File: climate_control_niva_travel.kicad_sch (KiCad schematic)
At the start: 12 parts, among them J2 SWD-отладка 1x04, U1 STM32F103RCT6

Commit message: реализована 2я занятость клетки
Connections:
- net LED_RECIRC_DRV is gone; now on net X_PWR/VCC_3V3: U1.10 (PC2)
- net X_SEN_CABIN/NTC_CABIN is gone; now on net X_PWR/VCC_3V3: U1.16 (PA2)
- net X_SEN_HEAT/NTC_HEAT is gone; now on net HEAT_FAN_PWM_CTL: U1.17 (PA3)
- net X_UI/LED_DRY_GLASS_DRV is gone; now on net HEAT_FAN_PWM_CTL: U1.3 (PC14)
- net HEAT_FAN_PWM_CTL: now also U1.2 (PC13)
- net X_M1/IN1: no longer U1.43 (PA10)
- net X_M2/IN1: no longer U1.45 (PA12)
- net X_M3/FB: no longer U1.27 (PB1)
- net X_M3/IN1: no longer U1.58 (PB6)
- net X_M4/IN1: no longer U1.2 (PC13)
- net X_UI/LED_DEFROST_GLASS_DRV: no longer C10.1, FB1.2, J2.2 (Pin_2), U1.13 (VDDA), U1.46 (PA13)
- net M_FAN_CTL renamed X_SEN_CABIN/M_FAN_CTL
- new net: C10.1, FB1.2, U1.13 (VDDA)
- new net: J2.2 (Pin_2), U1.46 (PA13)
- new net X_M1/IN2: U1.43 (PA10)
- new net X_M2/IN2: U1.45 (PA12)
- new net X_M3/IN2: U1.58 (PB6)
- new net X_M4/FB: U1.27 (PB1)

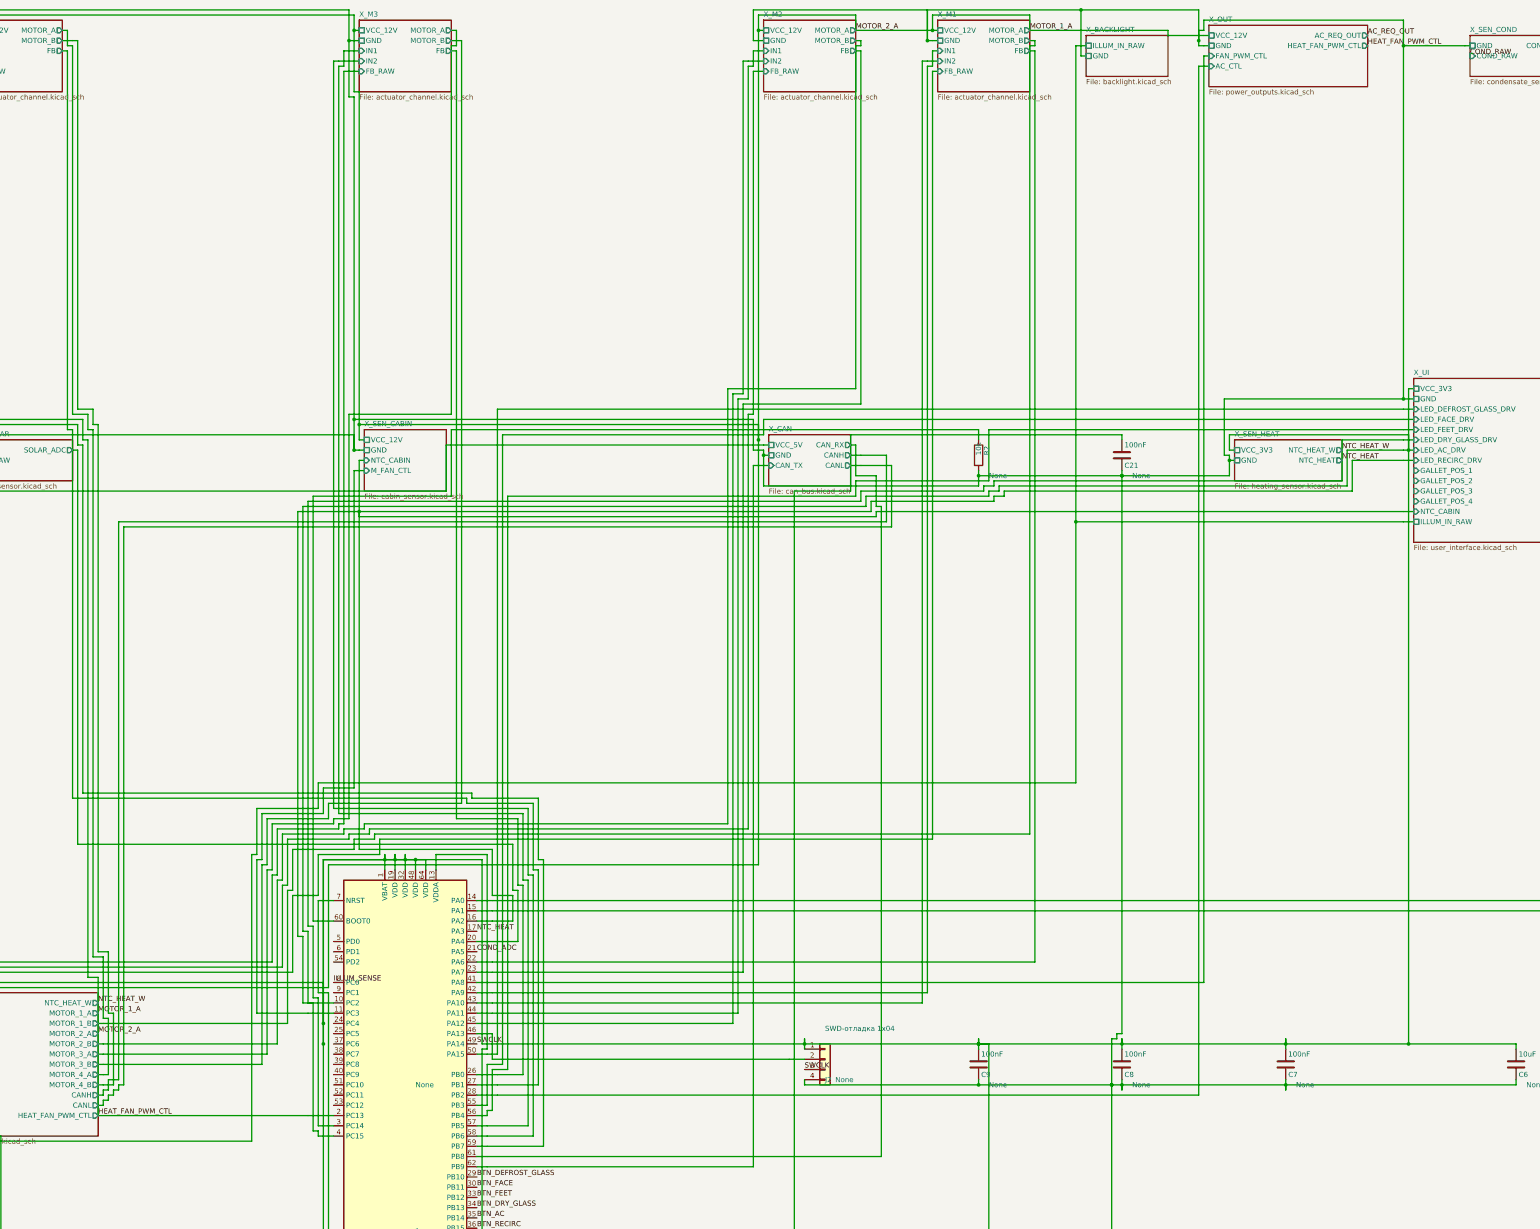
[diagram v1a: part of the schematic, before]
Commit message: фильтр клеток для Т если там пересечение
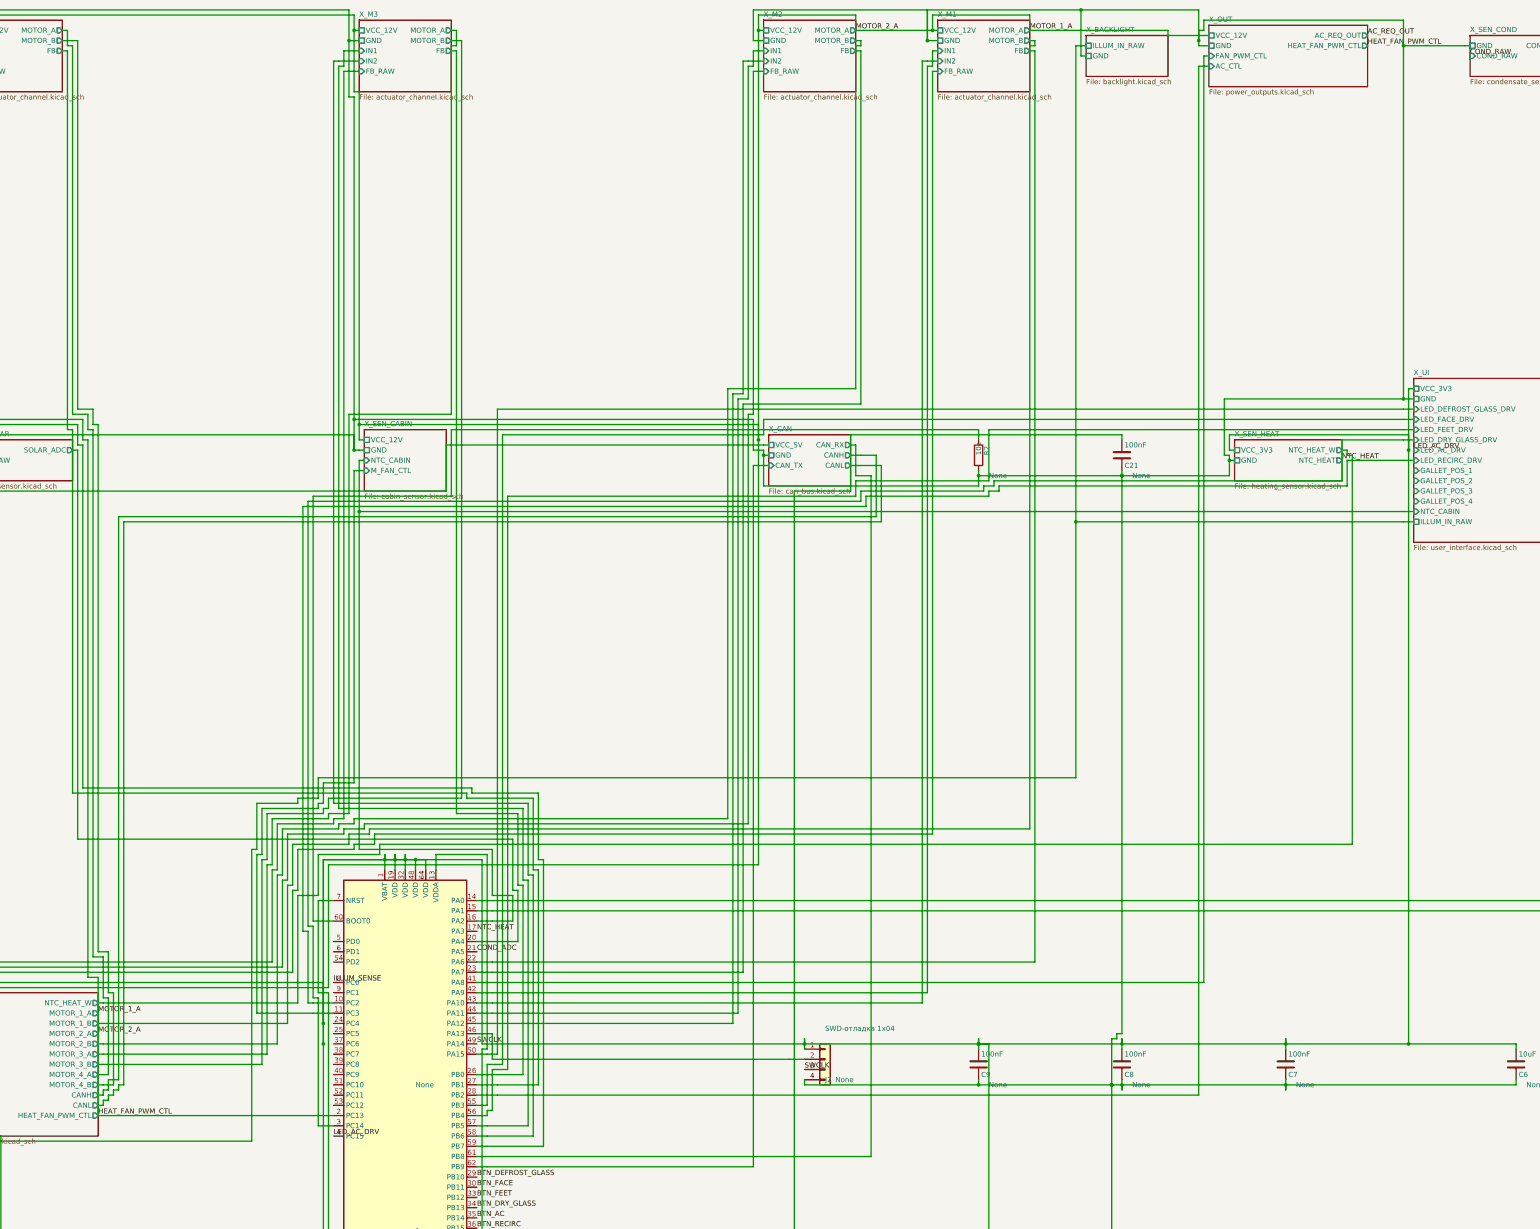
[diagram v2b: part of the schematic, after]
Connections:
- net HEAT_FAN_PWM_CTL: no longer U1.17 (PA3), U1.3 (PC14)
- net X_PWR/VCC_3V3: no longer U1.10 (PC2), U1.16 (PA2), U1.4 (PC15)
- new net LED_AC_DRV: U1.4 (PC15)
- new net NTC_HEAT: U1.17 (PA3), U1.3 (PC14)
- new net X_SEN_CABIN/NTC_CABIN: U1.16 (PA2)
- new net X_UI/LED_RECIRC_DRV: U1.10 (PC2)

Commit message: fic placer for small schemes
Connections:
- net NRST: now reaches C21.1, R1.2, U1.7 (NRST)
- net VDDA_3V3: now reaches C10.1, FB1.2, U1.13 (VDDA)
- net BOOT0: now reaches R2.1, U1.60 (BOOT0)
- net SWDIO: now reaches J2.2 (Pin_2), U1.46 (PA13)
- net NTC_HEAT renamed LED_DRY_GLASS_DRV
- net X_CAN/CAN_RX renamed CAN_RX
- net X_CAN/CAN_TX renamed CAN_TX
- net X_M1/FB renamed FB_M1
- net X_M1/IN1 renamed M1_IN1
- net X_M1/IN2 renamed M1_IN2
- net X_M2/FB renamed FB_M2
- net X_M2/IN1 renamed M2_IN1
- net X_M2/IN2 renamed M2_IN2
- net X_M3/FB renamed FB_M3
- net X_M3/IN1 renamed M3_IN1
- net X_M3/IN2 renamed M3_IN2
- net X_M4/FB renamed FB_M4
- net X_M4/IN1 renamed M4_IN1
- net X_OUT/AC_CTL renamed AC_CTL
- net X_OUT/FAN_PWM_CTL renamed FAN_PWM_CTL
- net X_PWR/VCC_3V3 renamed VCC_3V3
- net X_SEN_CABIN/M_FAN_CTL renamed M_FAN_CTL
- net X_SEN_CABIN/NTC_CABIN renamed NTC_CABIN
- net X_SEN_SOLAR/SOLAR_ADC renamed SOLAR_ADC
- net X_UI/FAN_SEL_ADC renamed FAN_SEL_ADC
- net X_UI/LED_DEFROST_GLASS_DRV renamed LED_DEFROST_GLASS_DRV
- net X_UI/LED_FACE_DRV renamed LED_FACE_DRV
- net X_UI/LED_FEET_DRV renamed LED_FEET_DRV
- net X_UI/LED_RECIRC_DRV renamed LED_RECIRC_DRV
- net X_UI/TEMP_SET_ADC renamed TEMP_SET_ADC

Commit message: all unit test pass
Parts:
- FB1: value Феррит 600Ом@100МГц по питанию VDDA -> Ferrite 600R@100MHz VDDA
- J2: value SWD-отладка 1x04 -> SWD debug 1x04
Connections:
- net HEAT_FAN_PWM_CTL renamed M4_IN2
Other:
- removed sheet X_CAN
- removed sheet X_M1
- removed sheet X_M2
- removed sheet X_M3
- removed sheet X_M4
- removed sheet X_OUT
- removed sheet X_PWR
- removed sheet X_SEN_CABIN
- removed sheet X_SEN_COND
- removed sheet X_SEN_HEAT
- removed sheet X_SEN_SOLAR
- removed sheet X_UI
- added sheet X_ACTUATOR_CHANNEL_M1 (actuator_channel.kicad_sch)
- added sheet X_ACTUATOR_CHANNEL_M2 (actuator_channel.kicad_sch)
- added sheet X_ACTUATOR_CHANNEL_M3 (actuator_channel.kicad_sch)
- added sheet X_ACTUATOR_CHANNEL_M4 (actuator_channel.kicad_sch)
- added sheet X_CABIN_SENSOR (cabin_sensor.kicad_sch)
- added sheet X_CAN_BUS (can_bus.kicad_sch)
- added sheet X_CONDENSATE_SENSOR (condensate_sensor.kicad_sch)
- added sheet X_HEATING_SENSOR (heating_sensor.kicad_sch)
- added sheet X_POWER_OUTPUTS (power_outputs.kicad_sch)
- added sheet X_POWER_SUPPLY (power_supply.kicad_sch)
- added sheet X_SOLAR_SENSOR (solar_sensor.kicad_sch)
- added sheet X_USER_INTERFACE (user_interface.kicad_sch)

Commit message: optimazed load to kicad
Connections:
- net M3_IN2 is gone; now on net FB_M4: U1.58 (PB6)
- net LED_DRY_GLASS_DRV: no longer U1.17 (PA3)
- net LED_FEET_DRV: now also U1.17 (PA3)

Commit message: tests_fix
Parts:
- removed U1: STM32F103RCT6, symbol MCU_ST_STM32F1:STM32F103R_C-D-E_Tx
- added U1: STM32G071RBT6, symbol MyMCU:STM32G071RBT6
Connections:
- net BOOT0 is gone; now on net SWCLK: R2.1
- net AC_CTL: now also U1.29 (PB2)
- net BTN_AC: now also U1.34 (PB14)
- net BTN_DEFROST_GLASS: now also U1.30 (PB10)
- net BTN_DRY_GLASS: now also U1.33 (PB13)
- net BTN_FACE: now also U1.31 (PB11)
- net BTN_FEET: now also U1.32 (PB12)
- net BTN_RECIRC: now also U1.35 (PB15)
- net CAN_RX: now also U1.62 (PB8)
- net CAN_TX: now also U1.63 (PB9)
- net COND_ADC: now also U1.22 (PA5)
- net FAN_PWM_CTL: now also U1.36 (PA8)
- net FAN_SEL_ADC: now also U1.16 (PC3), U1.18 (PA1)
- net FB_M1: now also U1.23 (PA6)
- net FB_M2: now also U1.24 (PA7)
- net FB_M3: now also U1.27 (PB0)
- net FB_M4: now also U1.28 (PB1)
- net GND: now also U1.9 (VSS/VSSA)
- net ILLUM_SENSE: now also U1.13 (PC0), U1.21 (PA4)
- net LED_AC_DRV: now also U1.5 (PC15-OSC32_OUT)
- net LED_DEFROST_GLASS_DRV: now also U1.47 (PA15)
- net LED_DRY_GLASS_DRV: now also U1.4 (PC14-OSC32_IN)
- net LED_FACE_DRV: now also U1.57 (PB3)
- net LED_FEET_DRV: now also U1.58 (PB4)
- net LED_RECIRC_DRV: now also U1.15 (PC2)
- net M1_IN1: now also U1.37 (PA9)
- net M1_IN2: now also U1.42 (PA10)
- net M2_IN1: now also U1.43 (PA11[PA9])
- net M2_IN2: now also U1.44 (PA12[PA10])
- net M3_IN1: now also U1.59 (PB5)
- net M4_IN1: now also U1.61 (PB7)
- net M4_IN2: now also U1.3 (PC13)
- net NRST: now also U1.12 (PF2-NRST)
- net NTC_CABIN: now also U1.19 (PA2)
- net SWCLK: now also U1.46 (PA14-BOOT0)
- net SWDIO: now also U1.45 (PA13)
- net TEMP_SET_ADC: now also U1.17 (PA0)
- net VCC_3V3: now also U1.6 (VBAT), U1.8 (VDD/VDDA)
- net VDDA_3V3: now also U1.7 (VREF+)
- new net M3_IN2: U1.60 (PB6)
- new net NTC_HEAT: U1.20 (PA3)
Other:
- title: (none) -> climate_control_niva_travel
